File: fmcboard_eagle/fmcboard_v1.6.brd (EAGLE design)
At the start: 147 x 74 mm, 294 parts, among them IC1 OPA699ID, IC10 LM358, IC11 7805DT, IC12 SN74AUC2G66DCTR, IC13 SN74AUC2G66DCTR, IC14 SN74AUC2G66DCTR, IC15 SN74AUC2G66DCTR, IC16 DAC7578SPWR, IC17 SN74AUC2G66DCTR, IC18 SN74AUC2G66DCTR, IC19 SN74AUC2G66DCTR, IC2 DAC7578SPWR, IC20 SN74AUC2G66DCTR, IC21 74AUP2GU04GW, IC22 74AUP2GU04GW, IC23 74AUP2GU04GW, IC24 74AUP2GU04GW, IC25 MC7905ACD2TR4G, IC26 AMS1117-1.8, IC27 LM358, IC28 SN74AUC2G66DCTR, IC29 LM337KVURG3, IC3 LTC6229IMS8E#TRPBF, IC30 SN74AUC2G66DCTR, IC31 SN74AUC2G66DCTR, IC32 SN74AUC2G66DCTR, IC33 LTC6229IMS8E#TRPBF, IC34 74AUP2GU04GW, IC35 74AUP2GU04GW, IC36 TPS5430DDAR, IC37 TPS5430DDAR, IC4 OPA695IDR, IC5 LTC6229IMS8E#TRPBF, IC6 OPA695IDR, IC7 OPA699ID, IC8 LM358, IC9 LM358, J1 8pin, J12 4p-2.54, J13 4p-2.54, J2 ASP-134604-01, J3 2p-2.54, J5 4p-2.54, J8 4p-2.54, J9 2p-2.54

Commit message: V holes
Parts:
- removed J3, J9: 2p-2.54, Seeed-Connector:H2-2.54
- added J4: 4p-2.54, Seeed-Connector:H4-2.54
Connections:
- net 12V: now also J4.1; no longer J9.1
- net 1V8: no longer J12.1
- net GND: now also J12.1, J4.3, J4.4; no longer J3.1, J3.2
- net VIN: now also J4.2; no longer J9.2
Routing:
- net VIN: track 68.5 -> 61.4 mm
- net GND: track 544.2 -> 547.8 mm, vias 125 -> 126
- net 12V: track 276.6 -> 273.8 mm
- net 1V8: track 212.3 -> 209.8 mm

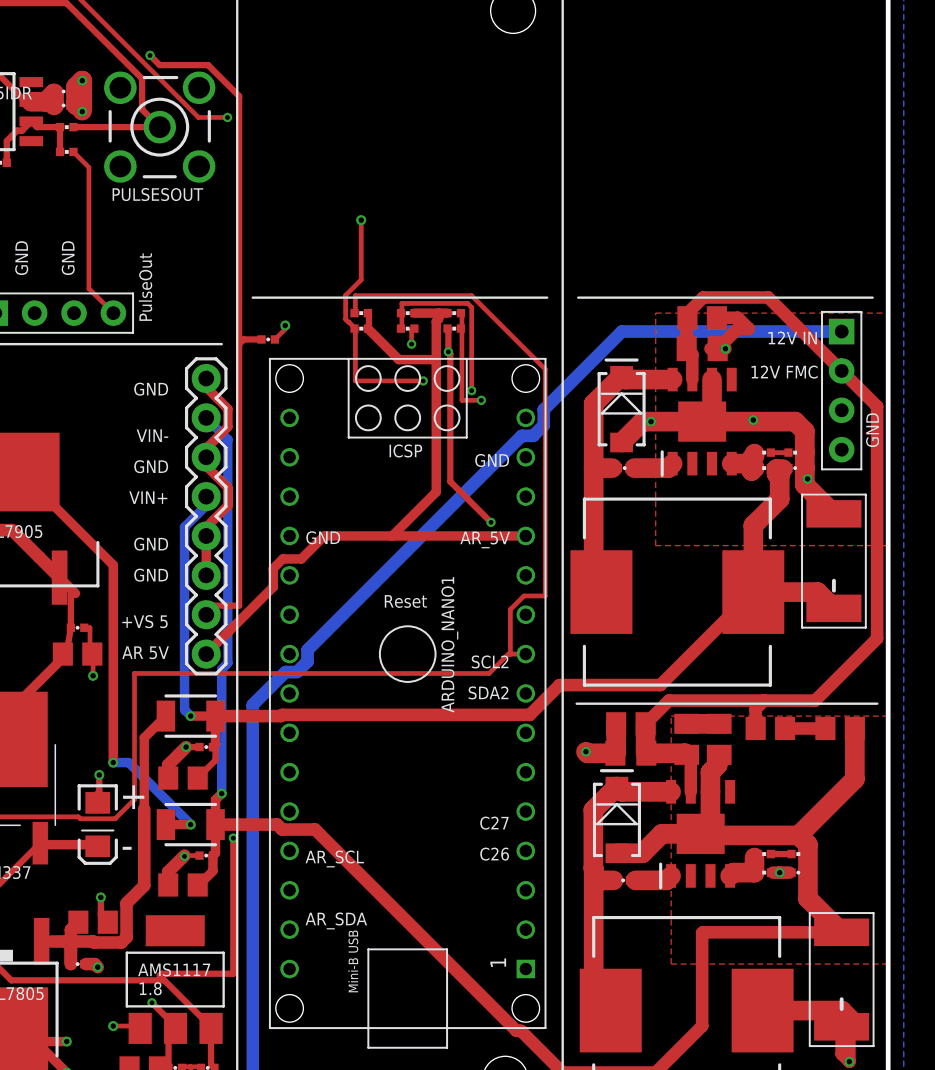
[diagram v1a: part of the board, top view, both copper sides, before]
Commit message: smd headers
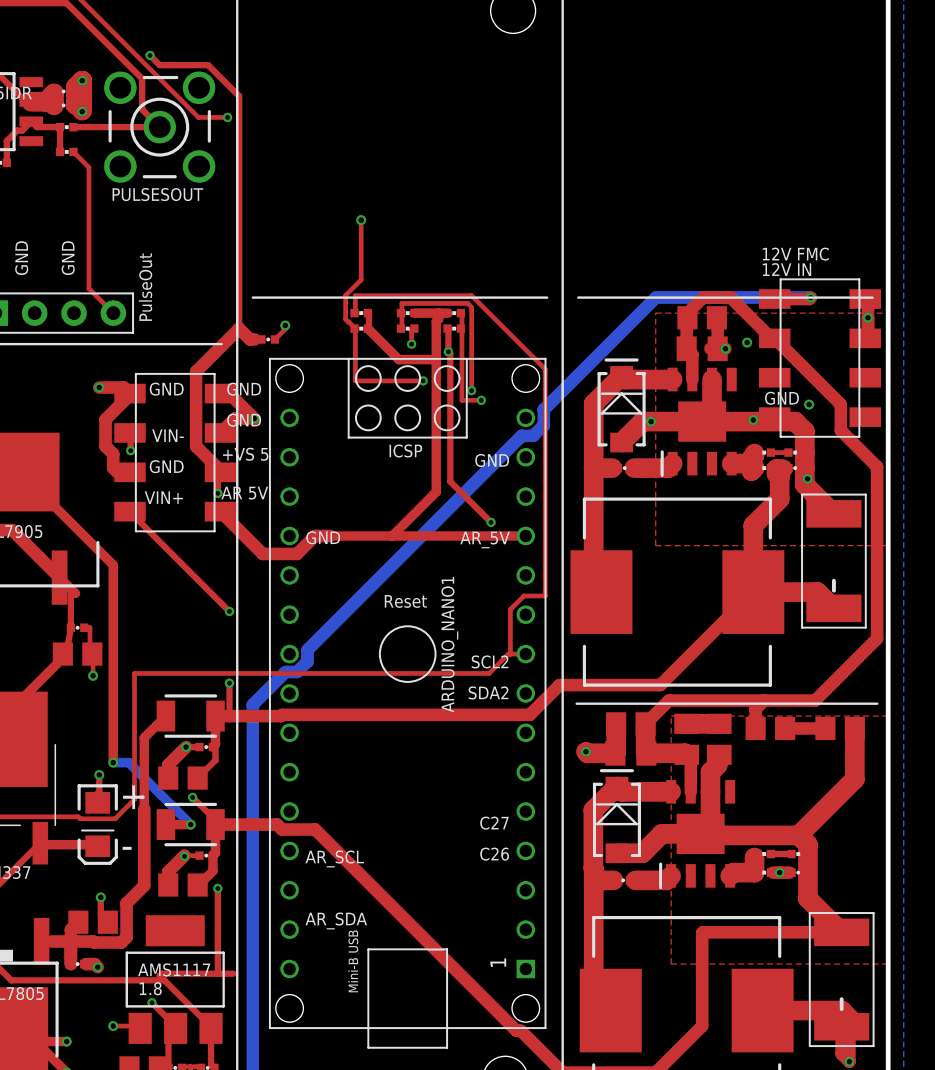
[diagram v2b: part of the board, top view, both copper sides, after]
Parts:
- removed J1: 8pin, SparkFun-Connectors:1X08
- removed J4: 4p-2.54, Seeed-Connector:H4-2.54
- added JP1, JP2: 8, pinhead+:2X04_SMT
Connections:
- net 12V: now also JP1.1; no longer J4.1
- net AR_5V: now also JP2.8; no longer J1.1
- net GND: now also JP1.2, JP1.4, JP1.5, JP1.6, JP1.7, JP1.8, JP2.1, JP2.2, JP2.4, JP2.5; no longer J1.3, J1.4, J1.6, J1.8, J4.3, J4.4
- net VIN: now also JP1.3; no longer J4.2
- net VIN+: now also JP2.7; no longer J1.5
- net VIN-: now also JP2.3; no longer J1.7
- net VS+: now also JP2.6; no longer J1.2
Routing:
- net AR_5V: track 48.5 -> 45.8 mm
- net VIN: track 61.4 -> 60.1 mm
- net 12V: track 273.8 -> 275.1 mm, vias 2 -> 3
- net GND: track 547.8 -> 548.7 mm, vias 126 -> 131
- net VIN+: track 75.0 -> 74.4 mm, vias 1 -> 2
- net VS+: track 384.1 -> 383.5 mm, vias 14 -> 15
- net VIN-: track 119.6 -> 120.0 mm, vias 1 -> 2

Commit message: Revert "smd headers"
This reverts commit 89ab3707157d78c83d60aa2d6a39565f5008c414.
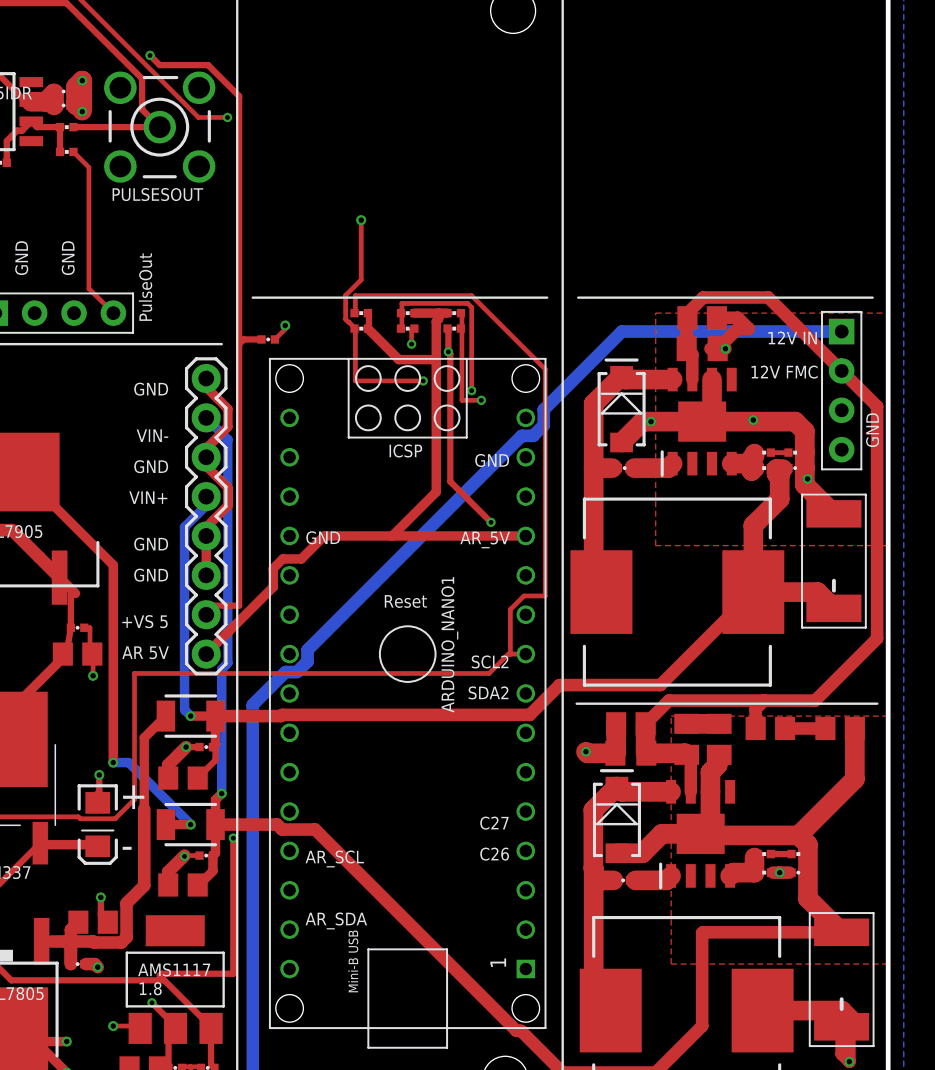
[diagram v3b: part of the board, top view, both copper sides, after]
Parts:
- removed JP1, JP2: 8, pinhead+:2X04_SMT
- added J1: 8pin, SparkFun-Connectors:1X08
- added J4: 4p-2.54, Seeed-Connector:H4-2.54
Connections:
- net 12V: now also J4.1; no longer JP1.1
- net AR_5V: now also J1.1; no longer JP2.8
- net GND: now also J1.3, J1.4, J1.6, J1.8, J4.3, J4.4; no longer JP1.2, JP1.4, JP1.5, JP1.6, JP1.7, JP1.8, JP2.1, JP2.2, JP2.4, JP2.5
- net VIN: now also J4.2; no longer JP1.3
- net VIN+: now also J1.5; no longer JP2.7
- net VIN-: now also J1.7; no longer JP2.3
- net VS+: now also J1.2; no longer JP2.6
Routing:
- net AR_5V: track 45.8 -> 48.5 mm
- net VIN: track 60.1 -> 61.4 mm
- net 12V: track 275.1 -> 273.8 mm, vias 3 -> 2
- net GND: track 548.7 -> 547.8 mm, vias 131 -> 126
- net VIN+: track 74.4 -> 75.0 mm, vias 2 -> 1
- net VS+: track 383.5 -> 384.1 mm, vias 15 -> 14
- net VIN-: track 120.0 -> 119.6 mm, vias 2 -> 1

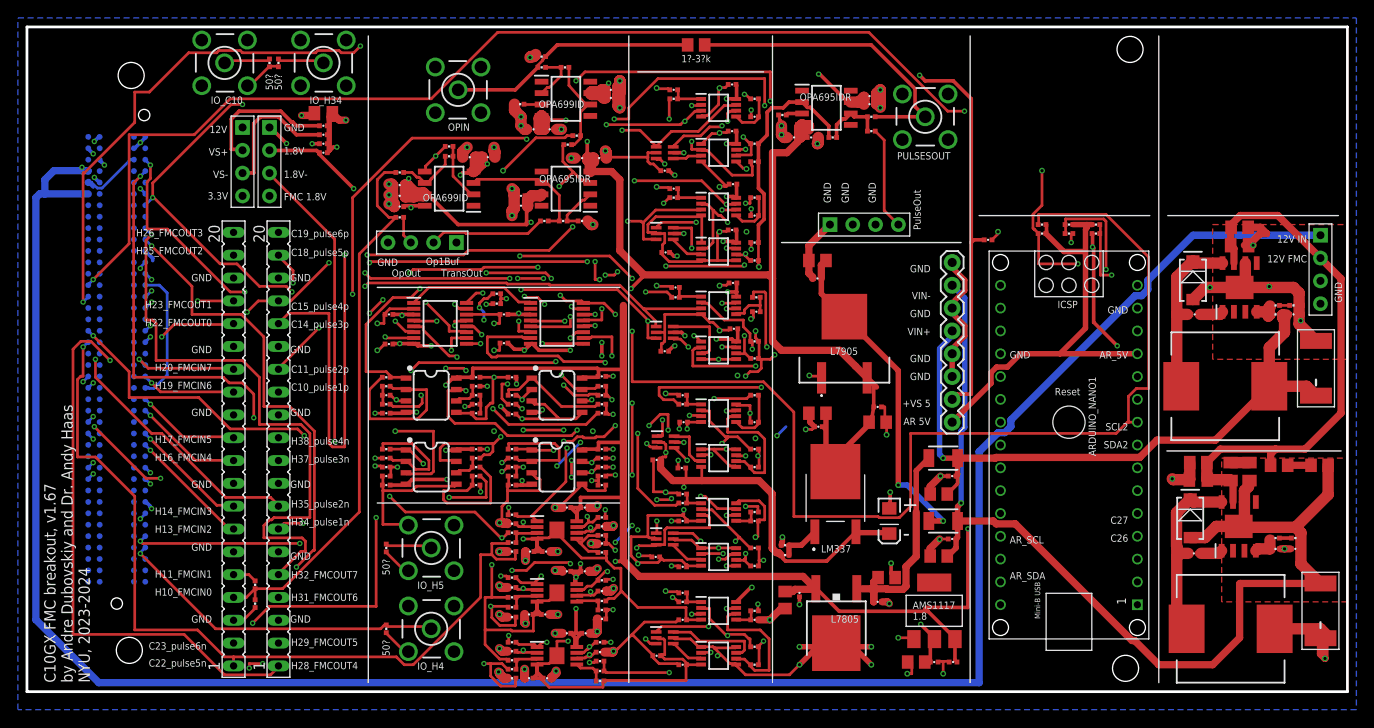
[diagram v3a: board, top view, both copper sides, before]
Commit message: connect 12V to VIN and AR_5V to VS+
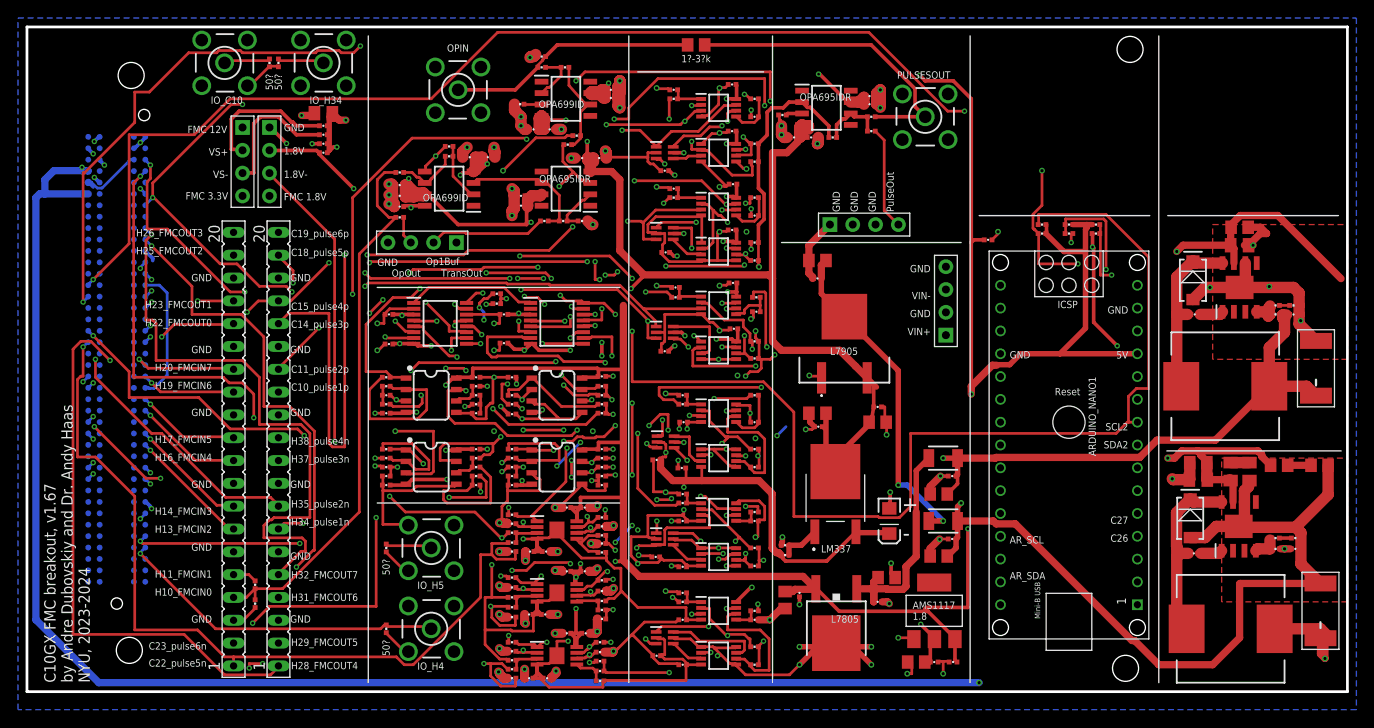
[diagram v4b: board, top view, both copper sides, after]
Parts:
- removed J4: 4p-2.54, Seeed-Connector:H4-2.54
- J1: value 8pin -> 4p-2.54; device SparkFun-Connectors:1X08 -> Seeed-Connector:H4-2.54
- moved J1 13.5 mm to (102.3, 43.5), turned to 180 degrees
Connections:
- removed net AR_5V: ARDUINO_NANO1.12, J1.1, R48.1, R49.1, R50.1, R51.1
- removed net VIN: C108.1, C11.1, C112.1, C64.1, C8.1, C80.1, IC36.7, IC37.7, J4.2
- net 12V: now also C108.1, C11.1, C112.1, C64.1, C8.1, C80.1, IC36.7, IC37.7; no longer J4.1
- net GND: now also J1.2; no longer J1.3, J1.6, J1.8, J4.3, J4.4
- net VIN+: now also J1.1; no longer J1.5
- net VIN-: now also J1.3; no longer J1.7
- net VS+: now also ARDUINO_NANO1.12, R48.1, R49.1, R50.1, R51.1; no longer J1.2
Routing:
- net VIN: track 61.4 -> 0.00 mm
- net AR_5V: track 48.5 -> 0.00 mm
- net VS+: track 384.1 -> 425.7 mm, vias 14 -> 15
- net 12V: track 273.8 -> 305.7 mm, vias 2 -> 5
- net GND: track 547.8 -> 533.1 mm
- net VIN+: track 75.0 -> 73.9 mm
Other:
- board text added: "5V"
- board text added: "FMC 12V"
- board text added: "FMC 3.3V"
- board text removed: "+VS 5"
- board text removed: "12V"
- board text removed: "12V FMC"
- board text removed: "12V IN"
- board text removed: "3.3V"
- board text removed: "AR 5V"
- board text removed: "AR_5V"

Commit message: minor routing
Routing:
- net 12V: track 305.7 -> 289.8 mm
- net GND: track 533.1 -> 535.2 mm
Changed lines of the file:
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@@
 <layer number="14" name="Route14" color="1" fill="6" visible="no" active="no"/>
 <layer number="15" name="route" color="19" fill="1" visible="yes" active="yes"/>
-<layer number="16" name="gnd" color="1" fill="1" visible="yes" active="yes"/>
+<layer number="16" name="gnd" color="1" fill="1" visible="no" active="yes"/>
 <layer number="17" name="Pads" color="2" fill="1" visible="yes" active="yes"/>
 <layer number="18" name="Vias" color="2" fill="1" visible="yes" active="yes"/>
@@
 <wire x1="141.6223" y1="43" x2="141.6223" y2="42" width="1.27" layer="1"/>
 <wire x1="141.6223" y1="42" x2="141.6223" y2="40.9257" width="1.27" layer="1"/>
-<wire x1="136.5" y1="49.7" x2="136" y2="49.7" width="0.8128" layer="1"/>
-<wire x1="136" y1="49.7" x2="135.53213125" y2="49.7" width="0.8128" layer="1"/>
 <wire x1="138.9" y1="7" x2="144" y2="7" width="1.27" layer="1"/>
 <wire x1="145" y1="6" x2="144" y2="7" width="1.27" layer="1"/>
-<polygon width="1.27" layer="1">
+<polygon width="0.4064" layer="1">
 <vertex x="146" y="37"/>
 <vertex x="132" y="37"/>
 <vertex x="132" y="52"/>
-<vertex x="147" y="52"/>
-<vertex x="147" y="37"/>
+<vertex x="146" y="52"/>
 </polygon>
 <via x="127.5" y="23.7" extent="1-16" drill="0.35"/>
@@
 <wire x1="141.43306875" y1="42" x2="141.6223" y2="42" width="0.3048" layer="1"/>
 <wire x1="141.43306875" y1="43" x2="141.6223" y2="43" width="0.3048" layer="1"/>
-<wire x1="135.5" y1="49.75" x2="136" y2="49.7" width="0.3048" layer="1"/>
 <wire x1="135.5" y1="49.75" x2="135.53213125" y2="49.7" width="0.3048" layer="1"/>
 <via x="76.875" y="4" extent="1-16" drill="0.3048"/>
@@
 <wire x1="129.4" y1="23.6" x2="127.6" y2="23.6" width="1.27" layer="1"/>
 <wire x1="127.6" y1="23.6" x2="127.5" y2="23.7" width="1.27" layer="1"/>
-<wire x1="136" y1="49.7" x2="137.3" y2="51" width="0.8128" layer="1"/>
-<wire x1="137.3" y1="51" x2="138" y2="51" width="0.8128" layer="1"/>
-<wire x1="138" y1="51" x2="137.3" y2="51.7" width="0.8128" layer="1"/>
-<wire x1="137.3" y1="51.7" x2="135.95" y2="51.7" width="0.8128" layer="1"/>
 <via x="96.2" y="14.3" extent="1-16" drill="0.35"/>
 <wire x1="96.2" y1="14.3" x2="96.2" y2="13.15" width="0.4064" layer="1"/>
@@
 <contactref element="J1" pad="2"/>
 <contactref element="J1" pad="4"/>
+<wire x1="135" y1="45" x2="135.95" y2="45.95" width="0.8128" layer="1"/>
+<wire x1="135" y1="45" x2="135" y2="46.4692375" width="0.8128" layer="1"/>
+<wire x1="135" y1="46.4692375" x2="135.3302" y2="46.7994375" width="0.8128" layer="1"/>
+<wire x1="135.3302" y1="51.0802" x2="135.95" y2="51.7" width="0.8128" layer="1"/>
+<wire x1="135.3302" y1="46.7994375" x2="135.3302" y2="51.0802" width="0.8128" layer="1"/>
 </signal>
 <signal name="IO1">
@@
 <wire x1="131.35" y1="25.5" x2="131.35" y2="23.65" width="1.27" layer="1"/>
 <wire x1="131.35" y1="23.65" x2="131.4" y2="23.6" width="1.27" layer="1"/>
-<wire x1="134" y1="49.7" x2="134" y2="51.65" width="0.8128" layer="1"/>
-<wire x1="134" y1="51.65" x2="134.05" y2="51.7" width="0.8128" layer="1"/>
-<wire x1="134" y1="52" x2="134" y2="51.75" width="0.8128" layer="1"/>
-<wire x1="134" y1="51.75" x2="134.05" y2="51.7" width="0.8128" layer="1"/>
 <contactref element="IC36" pad="7"/>
 <contactref element="IC37" pad="7"/>
@@
 <wire x1="134.265" y1="23.235" x2="134.265" y2="21.112" width="0.8128" layer="1"/>
 <wire x1="134.365" y1="49.335" x2="134.365" y2="47.712" width="0.8128" layer="1"/>
-<wire x1="134.0597375" y1="52" x2="134" y2="52" width="0.8128" layer="1"/>
-<wire x1="135.0685375" y1="53.0088" x2="134.0597375" y2="52" width="0.8128" layer="1"/>
-<wire x1="146.2888" y1="45.9812" x2="139.2612" y2="53.0088" width="0.8128" layer="1"/>
-<wire x1="139.2612" y1="53.0088" x2="135.0685375" y2="53.0088" width="0.8128" layer="1"/>
 <wire x1="134" y1="49.7" x2="134.365" y2="49.335" width="0.8128" layer="1"/>
 <wire x1="131.4" y1="23.6" x2="133.9" y2="23.6" width="0.8128" layer="1"/>
@@
 <wire x1="128" y1="49" x2="128.7" y2="49.7" width="0.8128" layer="1"/>
 <wire x1="128.7" y1="49.7" x2="134" y2="49.7" width="0.8128" layer="1"/>
+<wire x1="134" y1="49.7" x2="134" y2="51.65" width="0.8128" layer="1"/>
+<wire x1="134" y1="51.65" x2="134.05" y2="51.7" width="0.8128" layer="1"/>
 </signal>
 <signal name="TRANSOUT">
@@
 <wire x1="144.85" y1="25.2" x2="144.85" y2="21.9285" width="1.27" layer="1"/>
 <wire x1="144.85" y1="21.9285" x2="141.2215" y2="18.3" width="1.27" layer="1"/>
-<polygon width="1.27" layer="1">
-<vertex x="147" y="10"/>
+<polygon width="0.4064" layer="1">
+<vertex x="146" y="10"/>
 <vertex x="133" y="10"/>
 <vertex x="133" y="26"/>
-<vertex x="147" y="26"/>
+<vertex x="146" y="26"/>
 </polygon>
 <wire x1="103.6" y1="19" x2="107.58120625" y2="19" width="0.8128" layer="1"/>
